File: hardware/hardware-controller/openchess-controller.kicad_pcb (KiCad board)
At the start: 2 copper layers, 133.2 x 109.7 mm, 29 parts, among them J1 Conn_02x13, J3 J_PANEL XH-10, M1 Lipo Rider Plus, U2 ESP32-DevKitC, U3 74AHCT125, U6 TBD62783A

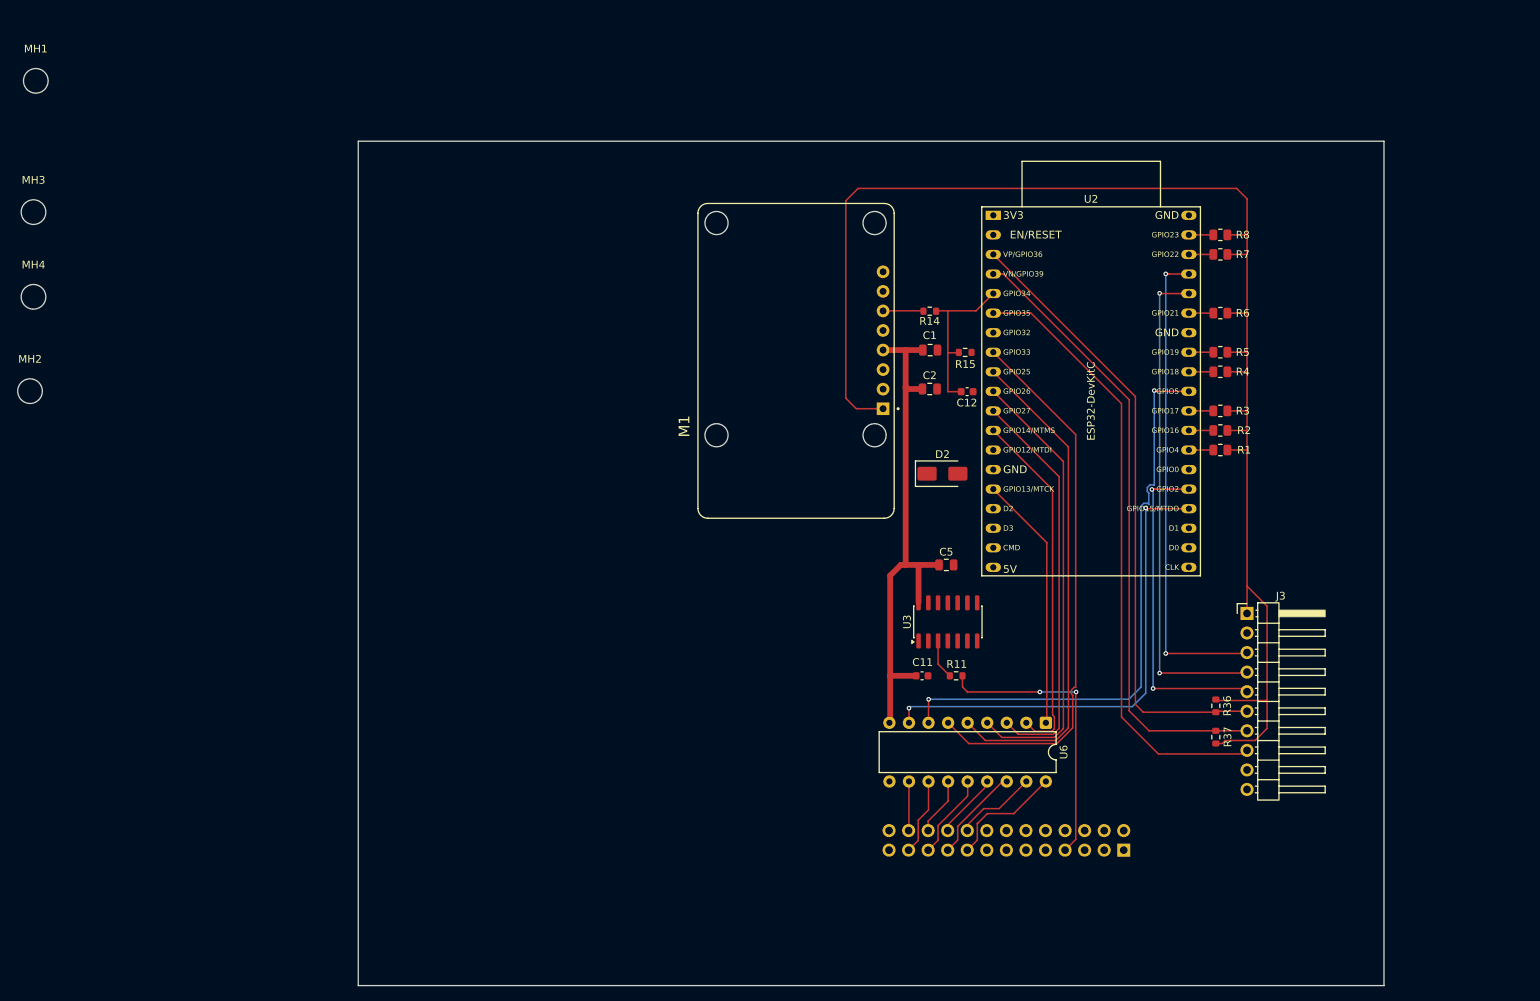
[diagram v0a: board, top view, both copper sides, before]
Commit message: Controller PCB: hand-routed power rails before autoroute
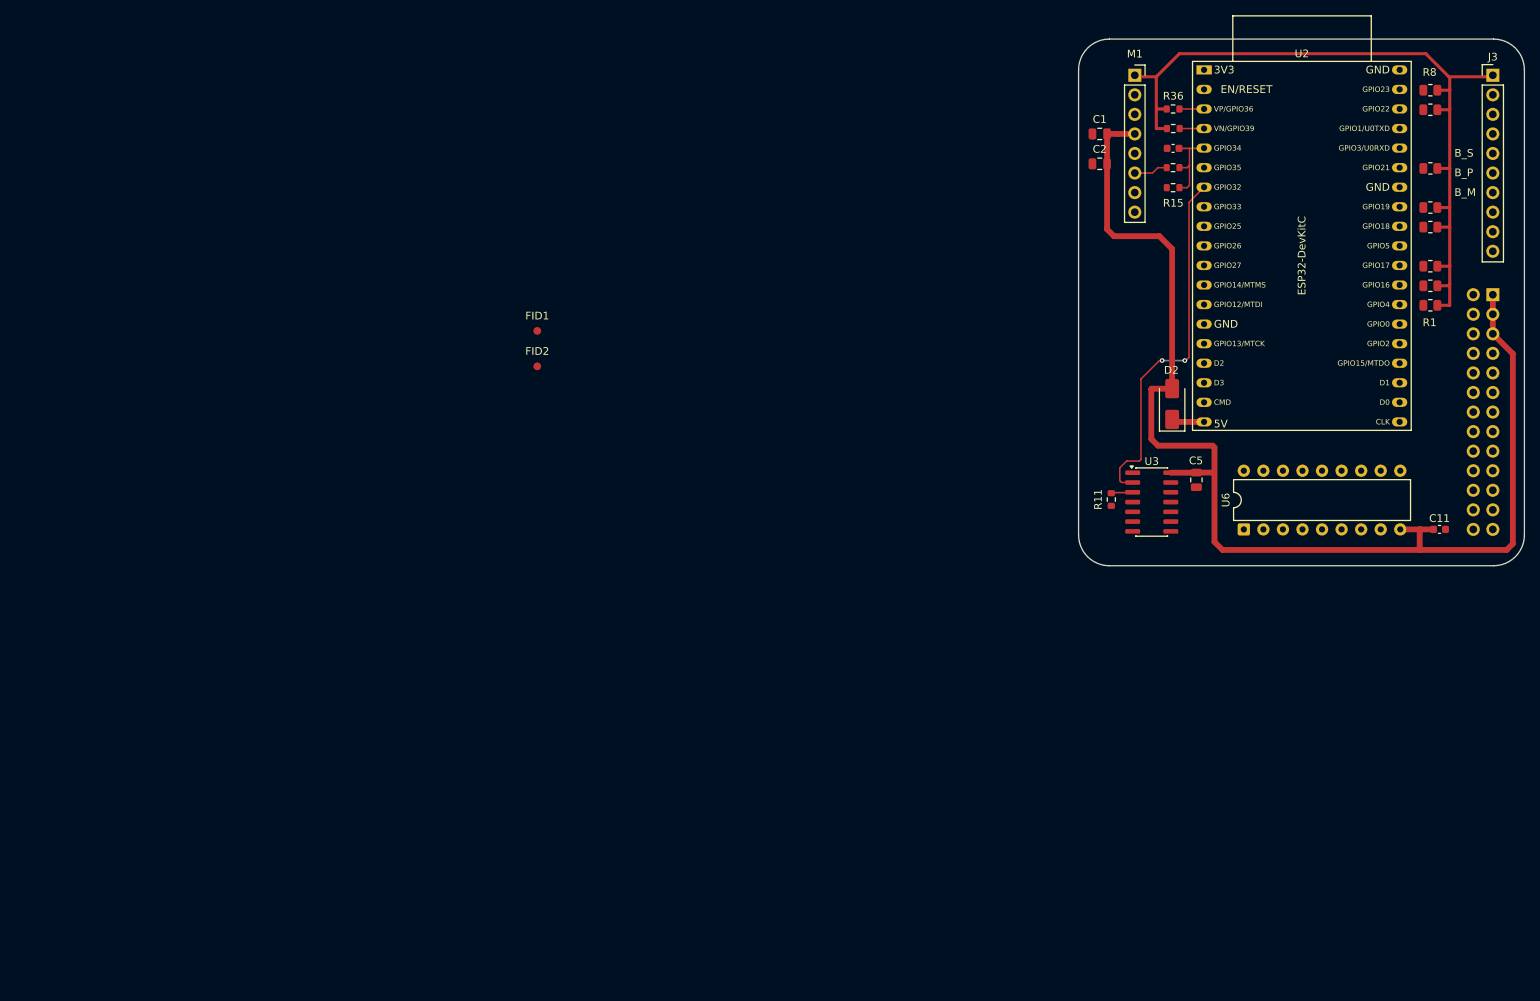
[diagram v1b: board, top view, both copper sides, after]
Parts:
- removed MH1, MH2, MH3, MH4: M3, MountingHole:MountingHole_3.2mm_M3
- added FID1: Fiducial, Fiducial:Fiducial_1mm_Mask2mm, F.Cu at (97.1, 68.5)
- added FID2: Fiducial, Fiducial:Fiducial_1mm_Mask2mm, F.Cu at (97.1, 73.1)
- J3: footprint Connector_PinHeader_2.54mm:PinHeader_1x10_P2.54mm_Horizontal -> Connector_PinHeader_2.54mm:PinHeader_1x10_P2.54mm_Vertical
- M1: footprint LipoRiderPlus:MODULE_106990290 -> Connector_PinSocket_2.54mm:PinSocket_1x08_P2.54mm_Vertical
- moved J1 86.6 mm to (221.2, 63.8), turned to 180 degrees
- moved R37 79.2 mm to (179.7, 42.2), turned to 0 degrees
- moved R36 77.7 mm to (179.7, 39.7), turned to 0 degrees
- moved J3 76.8 mm to (221.2, 35.3)
- moved C11 69.8 mm to (214.3, 94.3)
- moved M1 57.5 mm to (174.7, 35.3), turned to 0 degrees
- moved C12 41.4 mm to (179.7, 44.8), turned to 180 degrees
- moved R14 36.7 mm to (179.7, 47.3)
- moved C2 36.6 mm to (170.2, 46.8), turned to 180 degrees
- moved U6 35.9 mm to (188.9, 94.3), turned to 90 degrees
- moved C1 35.7 mm to (170.2, 42.9), turned to 180 degrees
- moved R15 34.4 mm to (179.7, 49.9), turned to 180 degrees
- moved C5 34.3 mm to (182.7, 87.8), turned to -90 degrees
- moved U2 33.3 mm to (183.7, 34.6)
- moved R1 33.1 mm to (213.1, 65.2)
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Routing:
- net +3.3V: track 192.7 -> 101.3 mm
- net +5V_LED: track 70.0 -> 159.2 mm
- net /PANEL_SPARE: track 80.7 -> 0.00 mm
- net /BTN_MODE: track 81.4 -> 3.17 mm
- net /BTN_POWER: track 81.0 -> 3.20 mm
- net /COL_DRV_G: track 76.2 -> 0.00 mm, vias 2 -> 0
- net /COL_DRV_F: track 71.8 -> 0.00 mm
- net /COL_DRV_E: track 65.0 -> 0.00 mm
- net /I2C_SCL: track 64.5 -> 0.00 mm, vias 2 -> 0
- net /COL_DRV_H: track 63.1 -> 0.00 mm, vias 2 -> 0
- net /I2C_SDA: track 62.9 -> 0.00 mm, vias 2 -> 0
- net /COL_DRV_D: track 58.7 -> 0.00 mm
- net /COL_DRV_C: track 52.5 -> 0.00 mm
- net /LED_DATA: track 0.00 -> 47.4 mm, vias 0 -> 2
- net /COL_DRV_B: track 46.3 -> 0.00 mm
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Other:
- board size 133.2 x 109.7 mm -> 57.9 x 68.4 mm
- board text added: "B_M"
- board text added: "B_P"
- board text added: "B_S"
- board text added: "R1"
- board text added: "R8"

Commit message: Add PCB layout and schematic guides for OpenChess controller
- Introduced `controller-PCB_LAYOUT_GUIDE.planning.md` detailing PCB layout constraints, component placement zones, net classes, routing priorities, and mechanical verification for the OpenChess controller.
- Added `controller-SCHEMATIC_GUIDE.planning.md` providing a comprehensive schematic specification, including reference designators, net lists, component details, and validation rules for the OpenChess controller PCB.
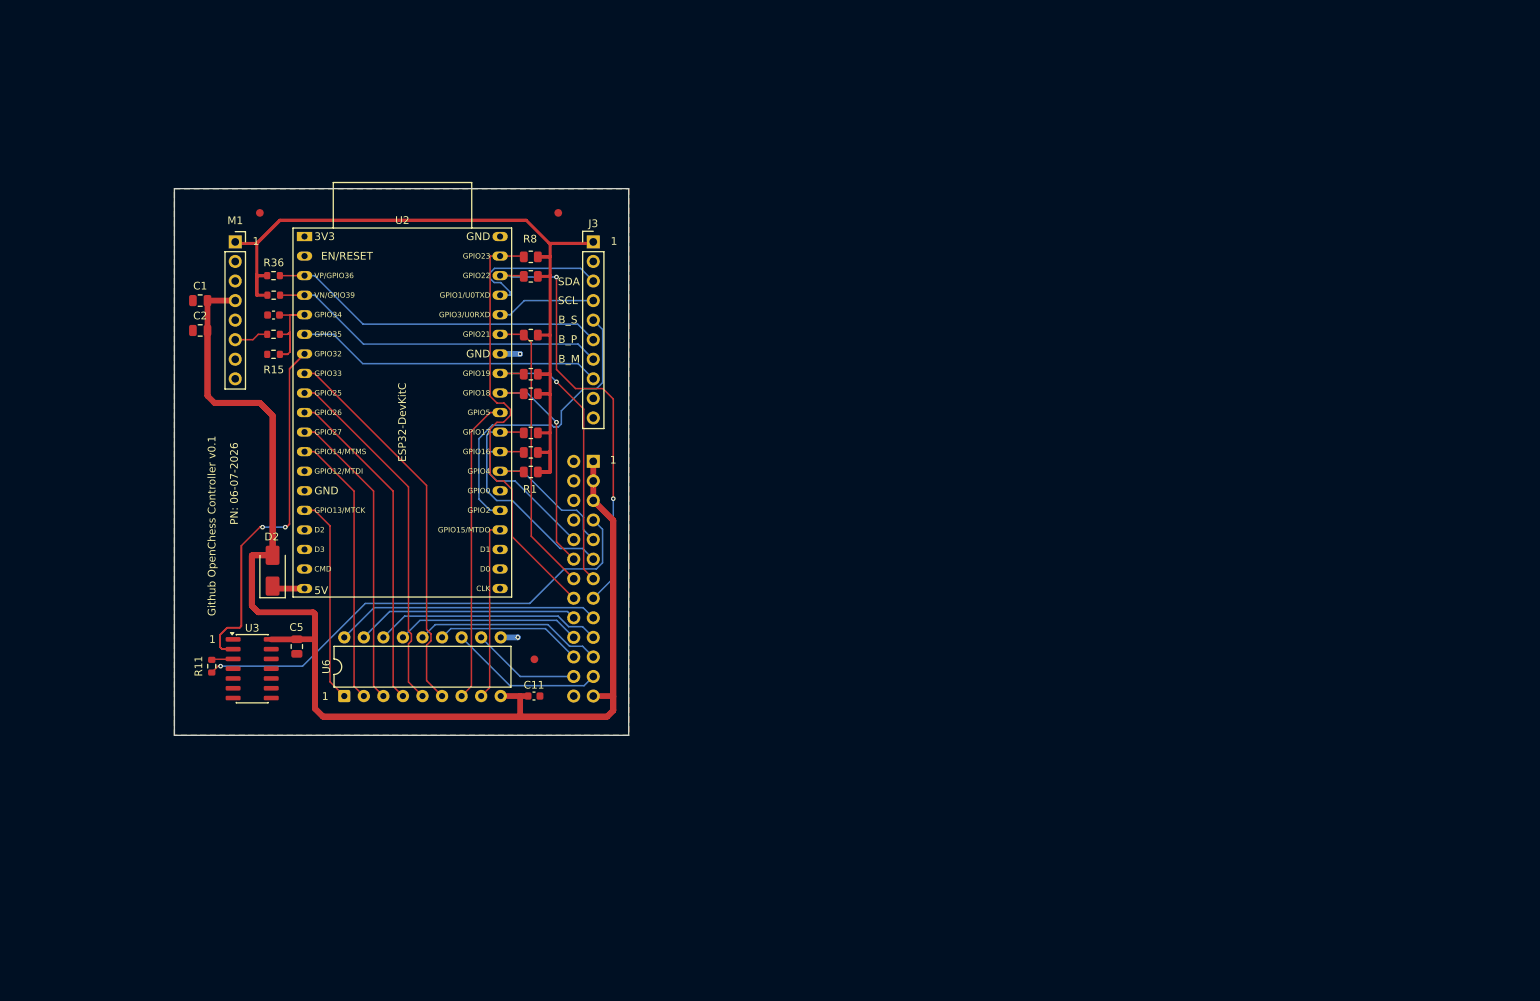
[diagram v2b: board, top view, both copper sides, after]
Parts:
- added FID3: Fiducial, Fiducial:Fiducial_1mm_Mask2mm, F.Cu at (96.8, 111.1)
- moved C11 119.6 mm to (96.7, 115.9)
- moved C2 118.8 mm to (53.3, 68.4)
- moved R11 118.8 mm to (54.8, 112.0)
- moved C5 118.8 mm to (65.9, 109.5)
- moved C1 118.8 mm to (53.3, 64.5)
- moved R1 118.8 mm to (96.3, 86.8)
- moved R2 118.8 mm to (96.3, 84.3)
- moved R3 118.8 mm to (96.3, 81.7)
- moved R4 118.8 mm to (96.3, 76.6)
- moved R5 118.8 mm to (96.3, 74.1)
- moved R6 118.8 mm to (96.3, 69.0)
- moved R7 118.8 mm to (96.3, 61.4)
- moved R8 118.8 mm to (96.3, 58.9)
- moved U3 118.8 mm to (60.1, 112.3)
- moved J1 118.8 mm to (104.4, 85.4)
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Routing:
- net +5V_LED: track 159.2 -> 286.9 mm
- net /LED_DATA_5V: track 0.00 -> 62.7 mm, vias 0 -> 1
- net /S6: track 0.00 -> 58.4 mm, vias 0 -> 2
- net /S7: track 0.00 -> 57.1 mm
- net +3.3V: track 101.3 -> 157.9 mm
- net /COL_DRV_F: track 0.00 -> 50.5 mm
- net /COL_DRV_E: track 0.00 -> 46.8 mm
- net /COL_DRV_D: track 0.00 -> 42.9 mm
- net /BTN_POWER: track 3.20 -> 44.1 mm
- net /BTN_MODE: track 3.17 -> 44.1 mm
- net /BTN_SELECT: track 0.00 -> 40.1 mm
- net /PANEL_SPARE: track 0.00 -> 39.9 mm
- net /COL_DRV_G: track 0.00 -> 39.7 mm
- net /COL_DRV_C: track 0.00 -> 39.3 mm
- net /S4: track 0.00 -> 38.4 mm, vias 0 -> 1
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- added copper zone on B.Cu, net GND
- added copper zone on F.Cu, net GND
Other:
- board size 57.9 x 68.4 mm -> 59 x 71 mm
- board text added: "1"
- board text added: "Github OpenChess Controller v0.1"
- board text added: "PN: 06-07-2026"
- board text added: "SCL"
- board text added: "SDA"

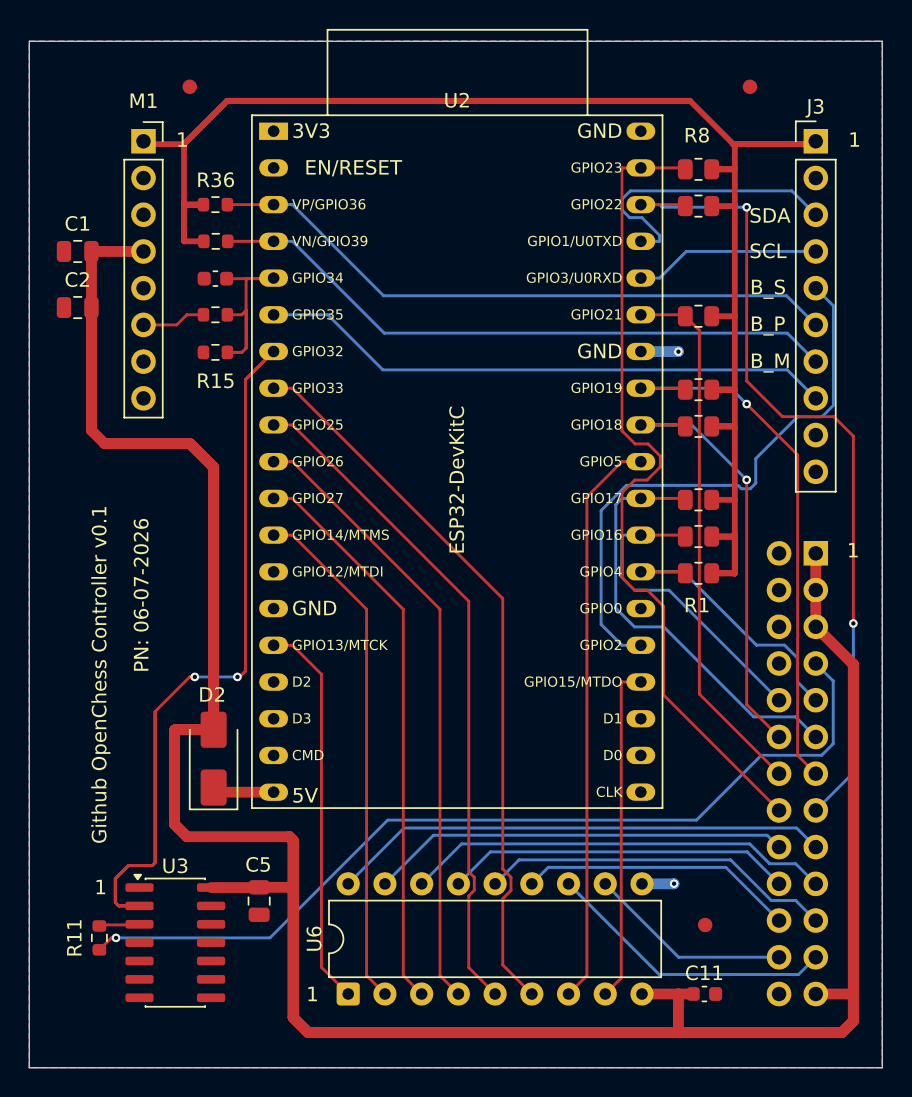
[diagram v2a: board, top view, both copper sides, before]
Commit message: Add initial files for openchess board project
- Created Gerber job file for openchess board with specifications and material stackup.
- Added backup of the KiCad PCB file before modifications.
- Introduced STEP files for the 3x3 chess board and the main chess controller.
- Initialized notes file for project documentation.
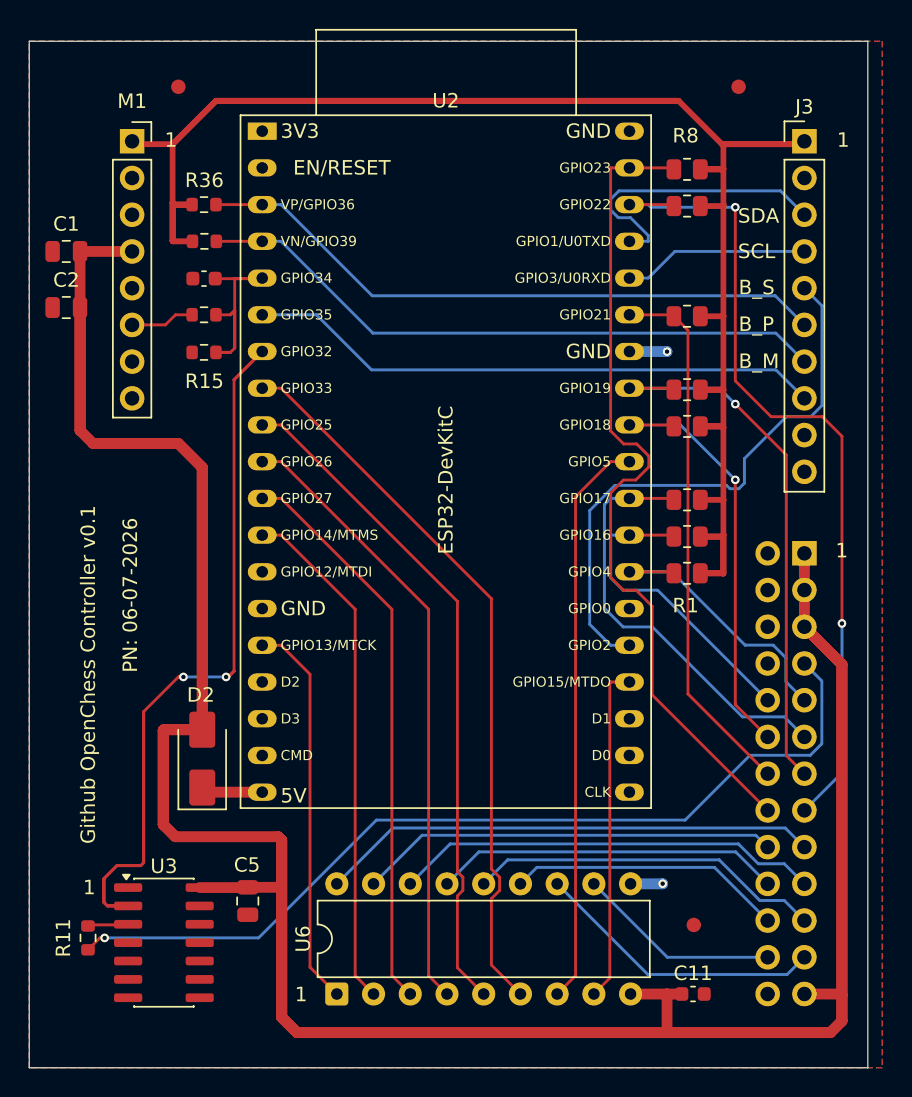
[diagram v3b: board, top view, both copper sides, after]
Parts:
- moved U6 0.79 mm to (71.3, 115.9)
- moved C12 0.79 mm to (62.1, 66.4)
- moved D2 0.79 mm to (62.0, 99.6)
- moved FID1 0.79 mm to (60.3, 53.1)
- moved M1 0.79 mm to (57.1, 56.9)
- moved R14 0.79 mm to (62.1, 68.9)
- moved R15 0.79 mm to (62.1, 71.5)
- moved R36 0.79 mm to (62.1, 61.3)
- moved R37 0.79 mm to (62.1, 63.8)
- moved C1 0.79 mm to (52.6, 64.5)
- moved C11 0.79 mm to (95.9, 115.9)
- moved C2 0.79 mm to (52.6, 68.4)
- moved C5 0.79 mm to (65.1, 109.5)
- moved FID2 0.79 mm to (99.1, 53.1)
- moved FID3 0.79 mm to (96.0, 111.1)
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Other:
- board size 59 x 71 mm -> 58 x 71 mm

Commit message: Add initial positions CSV for hardware components
This commit introduces a new CSV file containing the designator, midpoints, rotation, and layer information for various hardware components used in the project. The data includes positions for capacitors, resistors, diodes, and connectors, which are essential for the assembly and layout of the hardware.
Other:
- board text added: "Github PaoloJN Controller v0.1"
- board text removed: "Github OpenChess Controller v0.1"
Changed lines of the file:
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@@
 		(capping no)
 		(filling no)
-		(grid_origin 50 50)
+		(grid_origin 50 121)
 		(pcbplotparams
 			(layerselection 0x00000000_00000000_55555555_5755f5ff)
@@
 		(start 50 50)
 		(end 108 121)
+		(radius 3)
 		(stroke
 			(width 0.05)
@@
 		)
 	)
-	(gr_text "Github OpenChess Controller v0.1"
-		(at 54.6642 105.522817 90)
+	(gr_text "Github PaoloJN Controller v0.1"
+		(at 54.6642 103.85 90)
 		(layer "F.SilkS")
 		(effects
@@
 		)
 	)
+	(point
+		(at 50 121)
+		(size 1)
+		(layer "F.Cu")
+	)
 	(segment
